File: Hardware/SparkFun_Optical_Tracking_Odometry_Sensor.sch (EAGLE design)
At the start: 48 parts, among them J1 QWIIC_RIGHT_ANGLE, J2 QWIIC_RIGHT_ANGLE, Q1 100mA/20V/3.8Ω, Q2 100mA/20V/3.8Ω, U1 PAA5160, U2 LSM6DS0, U3 STM32C011F4U6, U4 RT9080-33GJ5

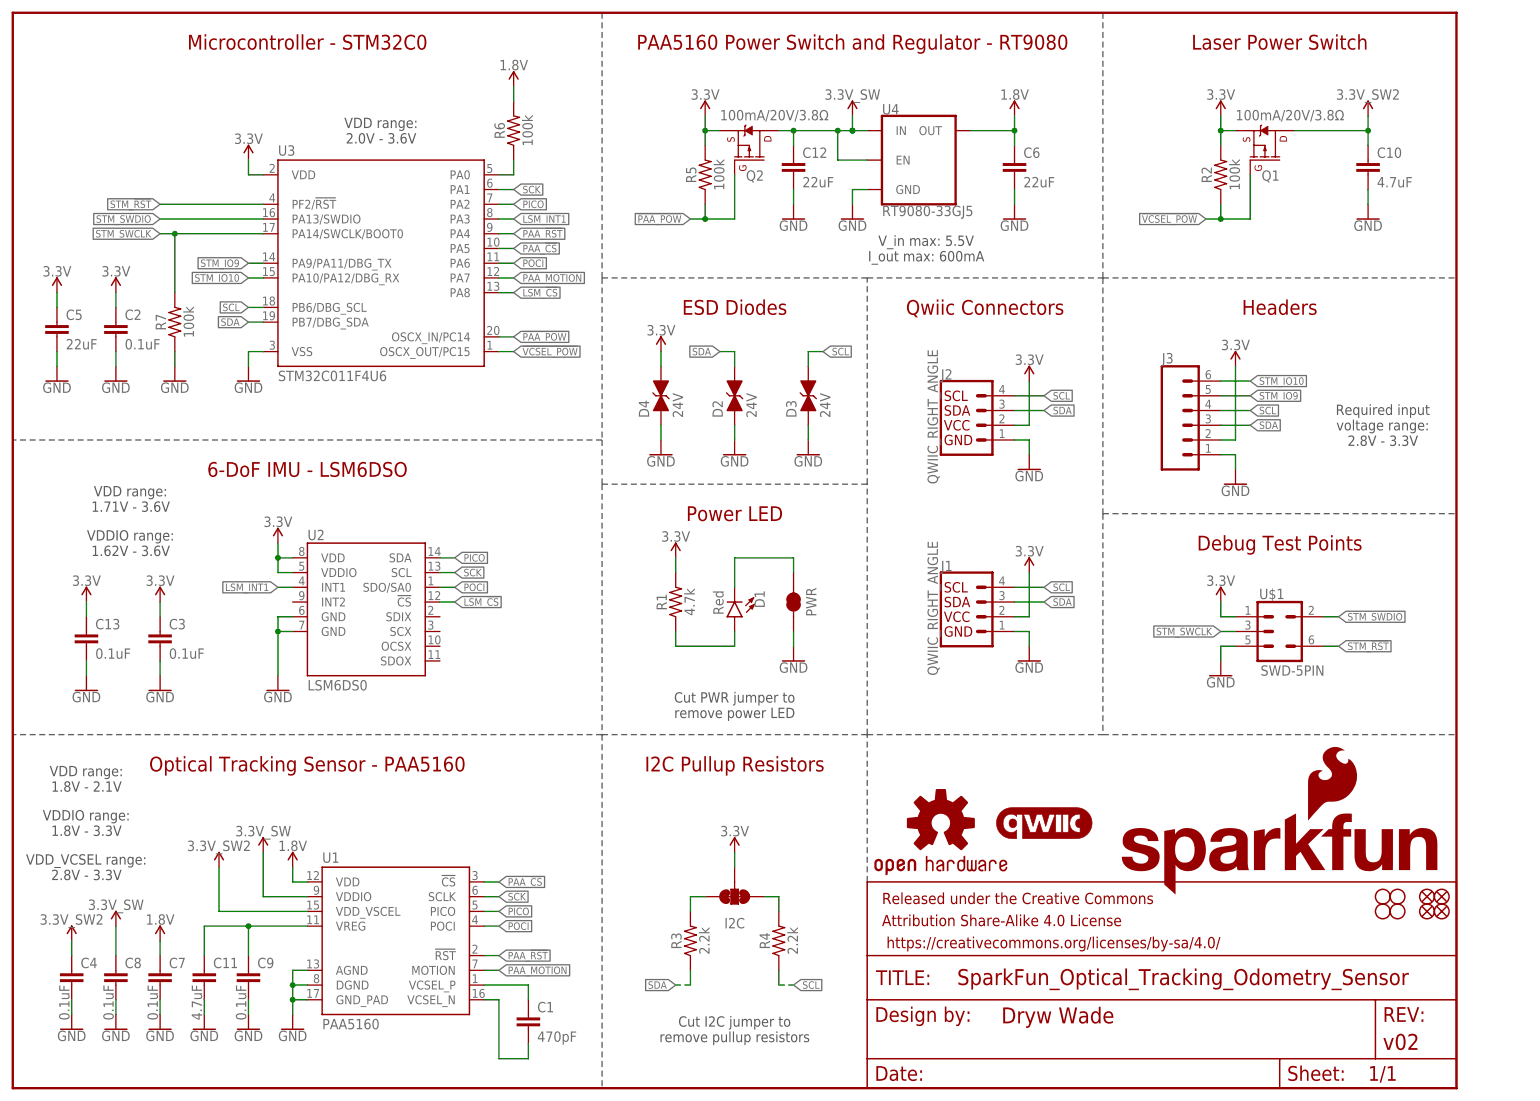
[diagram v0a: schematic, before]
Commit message: v10 updates
Bump version number to v10
Add external pullup to RST net
Nudge components and traces away from mounting holes
Replace 3.3V regulator with 1.8V version
Add PROD_ID values to STM32C0 and PAA5160
Rename PAA5160 to full name of PAA5160E1-Q
Rename STM32 to STM32C011F6U6 (32kB flash version)
Swap R6 for 1k to minimize effect of leakage current into ADC
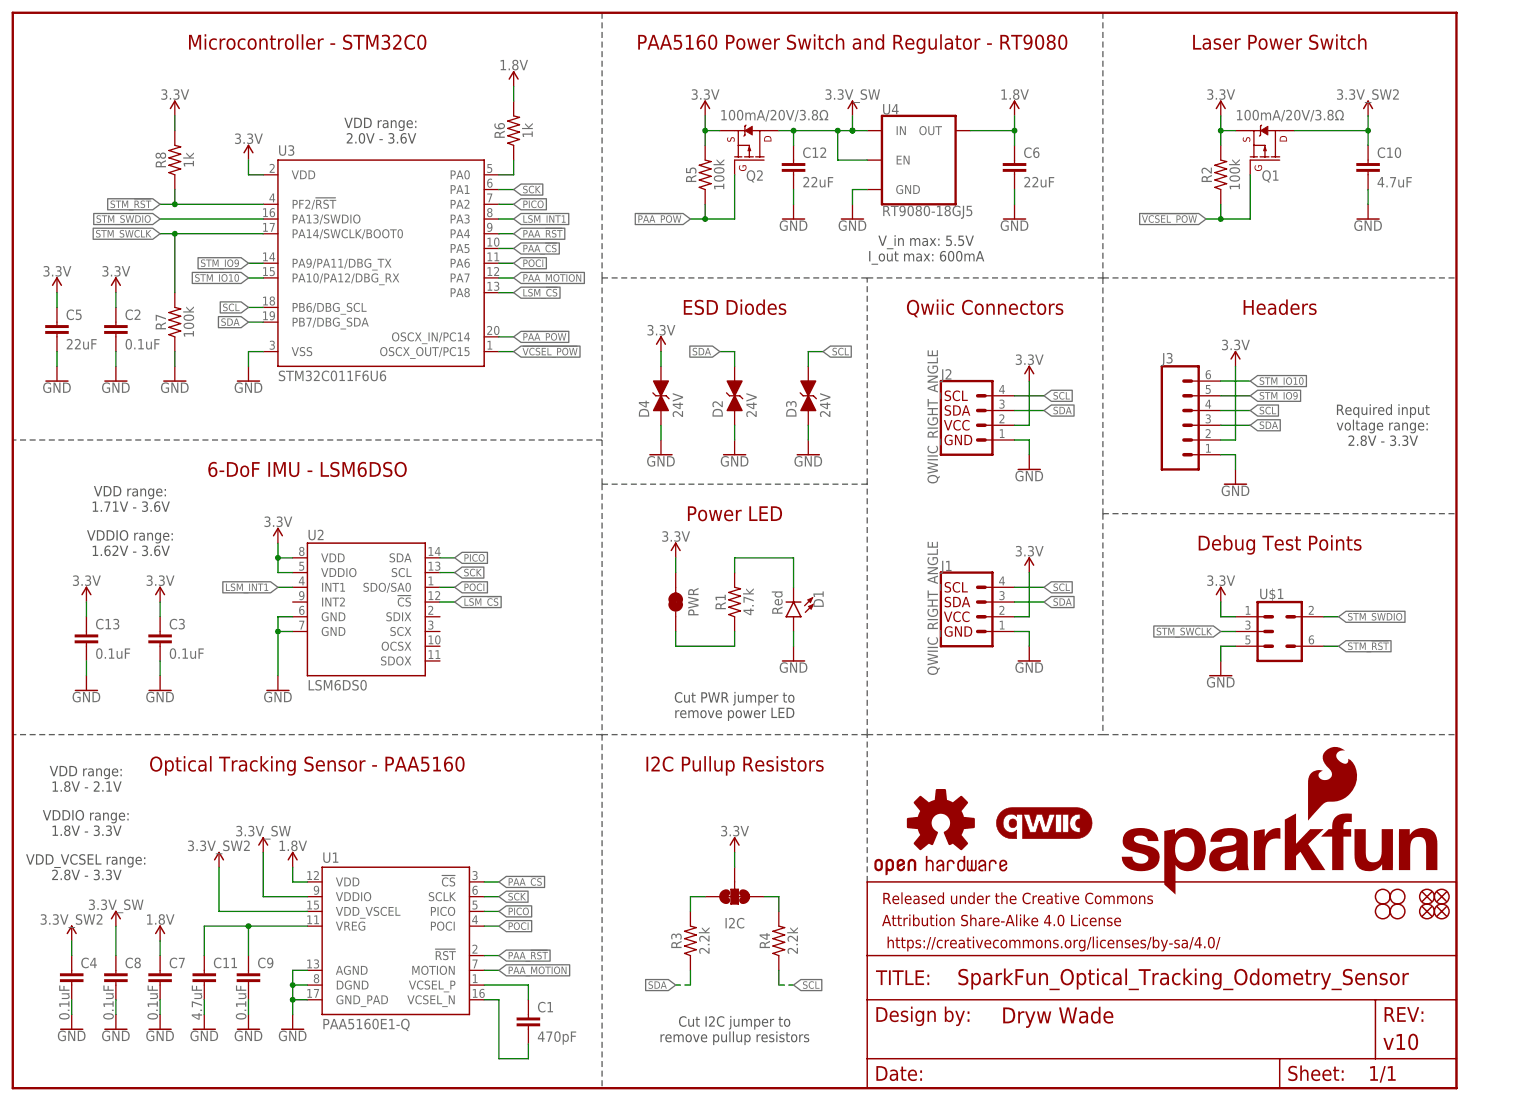
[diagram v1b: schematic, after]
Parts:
- added R8: 1k, SparkFun-Resistors:1KOHM-0603-1/10W-1%
- FRAME1: REV v02 -> v10
- R6: value 100k -> 1k; device SparkFun-Resistors:100KOHM-0603-1/10W-1% -> SparkFun-Resistors:1KOHM-0603-1/10W-1%
- U$1: value SWD-5PIN -> (none)
- U1: value PAA5160 -> PAA5160E1-Q; device Optical_Tracking_Odometry_Sensor:PAA5160 -> Optical_Tracking_Odometry_Sensor:PAA5160E1-Q
- U3: value STM32C011F4U6 -> STM32C011F6U6; device Optical_Tracking_Odometry_Sensor:STM32C011F4U6 -> Optical_Tracking_Odometry_Sensor:STM32C011F6U6
- U4: value RT9080-33GJ5 -> RT9080-18GJ5; device SparkFun-IC-Power:V_REG_RT9080 -> SparkFun-IC-Power:V_REG_RT9080-18GJ5
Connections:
- net 3.3V: now also PWR.2, R8.2; no longer R1.2
- net GND: now also D1.A; no longer PWR.1
- net N$1: now also PWR.1; no longer D1.A
- net N$2: now also R1.2; no longer PWR.2
- net STM_!RST!: now also R8.1
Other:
- moved on the sheet: D1, PWR, R1
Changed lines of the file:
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@@
 <part name="FRAME1" library="SparkFun-Aesthetics" deviceset="FRAME-LETTER" device="">
 <attribute name="DESIGNER" value="Dryw Wade"/>
-<attribute name="REV" value="v02"/>
+<attribute name="REV" value="v10"/>
 </part>
-<part name="U1" library="Optical_Tracking_Odometry_Sensor" deviceset="PAA5160" device=""/>
+<part name="U1" library="Optical_Tracking_Odometry_Sensor" deviceset="PAA5160E1-Q" device=""/>
 <part name="U2" library="SparkFun-Sensors" deviceset="LSM6DSO" device="" value="LSM6DS0"/>
 <part name="J1" library="SparkFun-Connectors" deviceset="QWIIC_CONNECTOR" device="JS-1MM" value="QWIIC_RIGHT_ANGLE"/>
@@
 <part name="H4" library="SparkFun-Hardware" deviceset="STAND-OFF" device=""/>
 <part name="J3" library="SparkFun-Connectors" deviceset="CONN_06" device="NO_SILK_NO_POP"/>
-<part name="U3" library="Optical_Tracking_Odometry_Sensor" deviceset="STM32C011F4U6" device=""/>
+<part name="U3" library="Optical_Tracking_Odometry_Sensor" deviceset="STM32C011F6U6" device=""/>
 <part name="GND1" library="SparkFun-PowerSymbols" deviceset="GND" device=""/>
 <part name="SUPPLY2" library="SparkFun-PowerSymbols" deviceset="1.8V" device=""/>
-<part name="U4" library="SparkFun-IC-Power" deviceset="V_REG_RT9080" device="" value="RT9080-33GJ5"/>
+<part name="U4" library="SparkFun-IC-Power" deviceset="V_REG_RT9080-18GJ5" device="" value="RT9080-18GJ5"/>
 <part name="SUPPLY4" library="SparkFun-PowerSymbols" deviceset="1.8V" device=""/>
 <part name="GND2" library="SparkFun-PowerSymbols" deviceset="GND" device=""/>
@@
 <part name="GND22" library="SparkFun-PowerSymbols" deviceset="GND" device=""/>
 <part name="SUPPLY25" library="SparkFun-PowerSymbols" deviceset="1.8V" device=""/>
-<part name="R6" library="SparkFun-Resistors" deviceset="100KOHM" device="-0603-1/10W-1%" value="100k"/>
+<part name="R6" library="SparkFun-Resistors" deviceset="1KOHM" device="-0603-1/10W-1%" value="1k"/>
 <part name="C5" library="SparkFun-Capacitors" deviceset="22UF" device="-0603-6.3V-20%" value="22uF"/>
 <part name="GND13" library="SparkFun-PowerSymbols" deviceset="GND" device=""/>
@@
 <part name="R7" library="SparkFun-Resistors" deviceset="100KOHM" device="-0603-1/10W-1%" value="100k"/>
 <part name="GND25" library="SparkFun-PowerSymbols" deviceset="GND" device=""/>
+<part name="R8" library="SparkFun-Resistors" deviceset="1KOHM" device="-0603-1/10W-1%" value="1k"/>
+<part name="SUPPLY26" library="SparkFun-PowerSymbols" deviceset="3.3V" device=""/>
 </parts>
 <sheets>
@@
 <instance part="FD3" gate="G$1" x="243.84" y="30.48" smashed="yes"/>
 <instance part="FD4" gate="G$1" x="243.84" y="33.02" smashed="yes"/>
-<instance part="D1" gate="G$1" x="124.46" y="81.28" smashed="yes" rot="R180">
-<attribute name="NAME" x="127.889" y="85.852" size="1.778" layer="95" font="vector" rot="R270"/>
-<attribute name="VALUE" x="122.555" y="85.852" size="1.778" layer="96" font="vector" rot="R270" align="top-left"/>
-</instance>
-<instance part="R1" gate="G$1" x="114.3" y="83.82" smashed="yes" rot="R90">
-<attribute name="NAME" x="112.776" y="83.82" size="1.778" layer="95" font="vector" rot="R90" align="bottom-center"/>
-<attribute name="VALUE" x="115.824" y="83.82" size="1.778" layer="96" font="vector" rot="R90" align="top-center"/>
-</instance>
-<instance part="PWR" gate="G$1" x="134.62" y="83.82" smashed="yes" rot="R90">
-<attribute name="NAME" x="137.668" y="83.82" size="1.778" layer="95" font="vector" rot="R270" align="center"/>
+<instance part="D1" gate="G$1" x="134.62" y="81.28" smashed="yes" rot="R180">
+<attribute name="NAME" x="138.049" y="85.852" size="1.778" layer="95" font="vector" rot="R270"/>
+<attribute name="VALUE" x="132.715" y="85.852" size="1.778" layer="96" font="vector" rot="R270" align="top-left"/>
+</instance>
+<instance part="R1" gate="G$1" x="124.46" y="83.82" smashed="yes" rot="R90">
+<attribute name="NAME" x="122.936" y="83.82" size="1.778" layer="95" font="vector" rot="R90" align="bottom-center"/>
+<attribute name="VALUE" x="125.984" y="83.82" size="1.778" layer="96" font="vector" rot="R90" align="top-center"/>
+</instance>
+<instance part="PWR" gate="G$1" x="114.3" y="83.82" smashed="yes" rot="R90">
+<attribute name="NAME" x="117.348" y="83.82" size="1.778" layer="95" font="vector" rot="R270" align="center"/>
 </instance>
 <instance part="SUPPLY10" gate="G$1" x="114.3" y="91.44" smashed="yes">
@@
 <instance part="GND25" gate="1" x="27.94" y="121.92" smashed="yes">
 <attribute name="VALUE" x="27.94" y="121.666" size="1.778" layer="96" font="vector" align="top-center"/>
+</instance>
+<instance part="R8" gate="G$1" x="27.94" y="160.02" smashed="yes" rot="R90">
+<attribute name="NAME" x="26.416" y="160.02" size="1.778" layer="95" font="vector" rot="R90" align="bottom-center"/>
+<attribute name="VALUE" x="29.464" y="160.02" size="1.778" layer="96" font="vector" rot="R90" align="top-center"/>
+</instance>
+<instance part="SUPPLY26" gate="G$1" x="27.94" y="167.64" smashed="yes">
+<attribute name="VALUE" x="27.94" y="170.434" size="1.778" layer="96" font="vector" align="bottom-center"/>
 </instance>
 </instances>
@@
 </segment>
 <segment>
-<pinref part="GND8" gate="1" pin="GND"/>
-<pinref part="PWR" gate="G$1" pin="1"/>
-<wire x1="134.62" y1="78.74" x2="134.62" y2="76.2" width="0.1524" layer="91"/>
-</segment>
-<segment>
 <pinref part="GND9" gate="1" pin="GND"/>
 <pinref part="U$1" gate="G$1" pin="5"/>
@@
 <pinref part="R7" gate="G$1" pin="1"/>
 <wire x1="27.94" y1="124.46" x2="27.94" y2="127" width="0.1524" layer="91"/>
+</segment>
+<segment>
+<pinref part="D1" gate="G$1" pin="A"/>
+<pinref part="GND8" gate="1" pin="GND"/>
+<wire x1="134.62" y1="78.74" x2="134.62" y2="76.2" width="0.1524" layer="91"/>
 </segment>
 </net>
@@
 </segment>
 <segment>
-<pinref part="SUPPLY10" gate="G$1" pin="3.3V"/>
-<pinref part="R1" gate="G$1" pin="2"/>
-<wire x1="114.3" y1="91.44" x2="114.3" y2="88.9" width="0.1524" layer="91"/>
-</segment>
-<segment>
 <pinref part="SUPPLY18" gate="G$1" pin="3.3V"/>
 <pinref part="I2C" gate="G$1" pin="2"/>
@@
 <wire x1="7.62" y1="137.16" x2="7.62" y2="134.62" width="0.1524" layer="91"/>
 </segment>
+<segment>
+<pinref part="R8" gate="G$1" pin="2"/>
+<pinref part="SUPPLY26" gate="G$1" pin="3.3V"/>
+<wire x1="27.94" y1="165.1" x2="27.94" y2="167.64" width="0.1524" layer="91"/>
+</segment>
+<segment>
+<pinref part="PWR" gate="G$1" pin="2"/>
+<pinref part="SUPPLY10" gate="G$1" pin="3.3V"/>
+<wire x1="114.3" y1="88.9" x2="114.3" y2="91.44" width="0.1524" layer="91"/>
+</segment>
 </net>
 <net name="LSM_!CS!" class="0">
@@
 <segment>
 <pinref part="U3" gate="G$1" pin="PF2/!RST!"/>
-<wire x1="43.18" y1="152.4" x2="25.4" y2="152.4" width="0.1524" layer="91"/>
+<wire x1="43.18" y1="152.4" x2="27.94" y2="152.4" width="0.1524" layer="91"/>
 <label x="25.4" y="152.4" size="1.27" layer="95" font="vector" rot="R180" xref="yes"/>
+<pinref part="R8" gate="G$1" pin="1"/>
+<wire x1="27.94" y1="152.4" x2="25.4" y2="152.4" width="0.1524" layer="91"/>
+<wire x1="27.94" y1="154.94" x2="27.94" y2="152.4" width="0.1524" layer="91"/>
+<junction x="27.94" y="152.4"/>
 </segment>
 <segment>
@@
 <label x="40.64" y="142.24" size="1.27" layer="95" font="vector" rot="R180" xref="yes"/>
 <pinref part="U3" gate="G$1" pin="PA9/PA11/DBG_TX"/>
-</segment>
-</net>
-<net name="N$1" class="0">
-<segment>
-<pinref part="R1" gate="G$1" pin="1"/>
-<pinref part="D1" gate="G$1" pin="A"/>
-<wire x1="124.46" y1="78.74" x2="124.46" y2="76.2" width="0.1524" layer="91"/>
-<wire x1="124.46" y1="76.2" x2="114.3" y2="76.2" width="0.1524" layer="91"/>
-<wire x1="114.3" y1="76.2" x2="114.3" y2="78.74" width="0.1524" layer="91"/>
-</segment>
-</net>
-<net name="N$2" class="0">
-<segment>
-<pinref part="D1" gate="G$1" pin="C"/>
-<pinref part="PWR" gate="G$1" pin="2"/>
-<wire x1="124.46" y1="86.36" x2="124.46" y2="91.44" width="0.1524" layer="91"/>
-<wire x1="124.46" y1="91.44" x2="134.62" y2="91.44" width="0.1524" layer="91"/>
-<wire x1="134.62" y1="91.44" x2="134.62" y2="88.9" width="0.1524" layer="91"/>
 </segment>
 </net>
@@
 </segment>
 </net>
+<net name="N$1" class="0">
+<segment>
+<pinref part="PWR" gate="G$1" pin="1"/>
+<wire x1="114.3" y1="78.74" x2="114.3" y2="76.2" width="0.1524" layer="91"/>
+<pinref part="R1" gate="G$1" pin="1"/>
+<wire x1="114.3" y1="76.2" x2="124.46" y2="76.2" width="0.1524" layer="91"/>
+<wire x1="124.46" y1="76.2" x2="124.46" y2="78.74" width="0.1524" layer="91"/>
+</segment>
+</net>
+<net name="N$2" class="0">
+<segment>
+<pinref part="R1" gate="G$1" pin="2"/>
+<wire x1="124.46" y1="88.9" x2="124.46" y2="91.44" width="0.1524" layer="91"/>
+<pinref part="D1" gate="G$1" pin="C"/>
+<wire x1="124.46" y1="91.44" x2="134.62" y2="91.44" width="0.1524" layer="91"/>
+<wire x1="134.62" y1="91.44" x2="134.62" y2="86.36" width="0.1524" layer="91"/>
+</segment>
+</net>

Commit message: Update section titles in schematic
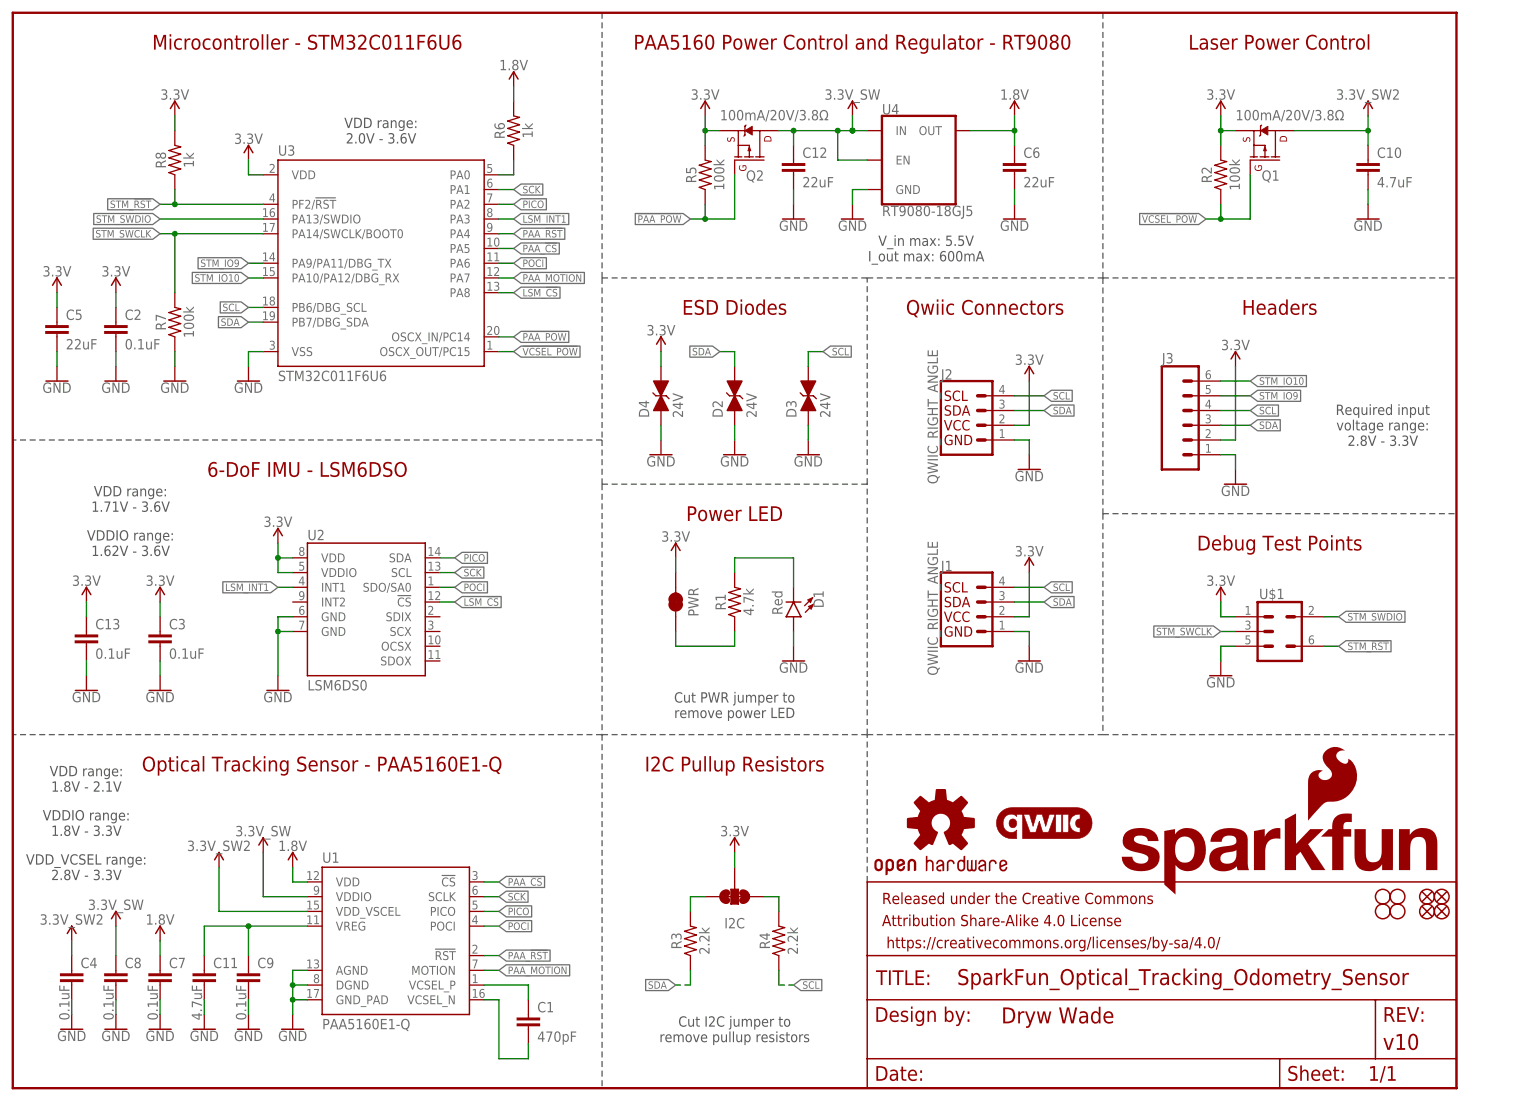
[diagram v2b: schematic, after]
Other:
- note added: "Laser Power Control"
- note added: "Microcontroller - STM32C011F6U6"
- note added: "Optical Tracking Sensor - PAA5160E1-Q"
- note added: "PAA5160 Power Control and Regulator - RT9080"
- note removed: "Laser Power Switch"
- note removed: "Microcontroller - STM32C0"
- note removed: "Optical Tracking Sensor - PAA5160"
- note removed: "PAA5160 Power Switch and Regulator - RT9080"
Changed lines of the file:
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@@
 <wire x1="187.96" y1="139.7" x2="187.96" y2="185.42" width="0.2032" layer="97" style="longdash"/>
 <text x="124.46" y="99.06" size="2.54" layer="94" font="vector" align="center">Power LED</text>
-<text x="50.8" y="55.88" size="2.54" layer="94" font="vector" align="center">Optical Tracking Sensor - PAA5160</text>
+<text x="53.34" y="55.88" size="2.54" layer="94" font="vector" align="center">Optical Tracking Sensor - PAA5160E1-Q</text>
 <text x="50.8" y="106.68" size="2.54" layer="94" font="vector" align="center">6-DoF IMU - LSM6DSO</text>
-<text x="50.8" y="180.34" size="2.54" layer="94" font="vector" align="center">Microcontroller - STM32C0</text>
-<text x="144.78" y="180.34" size="2.54" layer="94" font="vector" align="center">PAA5160 Power Switch and Regulator - RT9080</text>
+<text x="50.8" y="180.34" size="2.54" layer="94" font="vector" align="center">Microcontroller - STM32C011F6U6</text>
+<text x="144.78" y="180.34" size="2.54" layer="94" font="vector" align="center">PAA5160 Power Control and Regulator - RT9080</text>
 <text x="218.44" y="93.98" size="2.54" layer="94" font="vector" align="center">Debug Test Points</text>
 <text x="167.64" y="134.62" size="2.54" layer="94" font="vector" align="center">Qwiic Connectors</text>
@@
 <wire x1="187.96" y1="99.06" x2="248.92" y2="99.06" width="0.2032" layer="97" style="longdash"/>
 <wire x1="101.6" y1="104.14" x2="147.32" y2="104.14" width="0.2032" layer="97" style="longdash"/>
-<text x="218.44" y="180.34" size="2.54" layer="94" font="vector" align="center">Laser Power Switch</text>
+<text x="218.44" y="180.34" size="2.54" layer="94" font="vector" align="center">Laser Power Control</text>
 <text x="157.48" y="144.78" size="1.778" layer="97" font="vector" align="center">V_in max: 5.5V
 I_out max: 600mA</text>
